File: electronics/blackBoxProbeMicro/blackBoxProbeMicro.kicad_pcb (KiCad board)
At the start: 4 copper layers, 29 x 29 mm, 60 parts, among them J1 USB-C, J2 JTAG_2X05, J3 JTAG_2X05, J4 DevBoardUartOutput, Q1 Q_NMOS_DUAL, Q2 Q_PMOS_DUAL, U1 MCP1702-MB, U2 USBLC6-2, U3 STM32F103CBT, Y1 8MHz

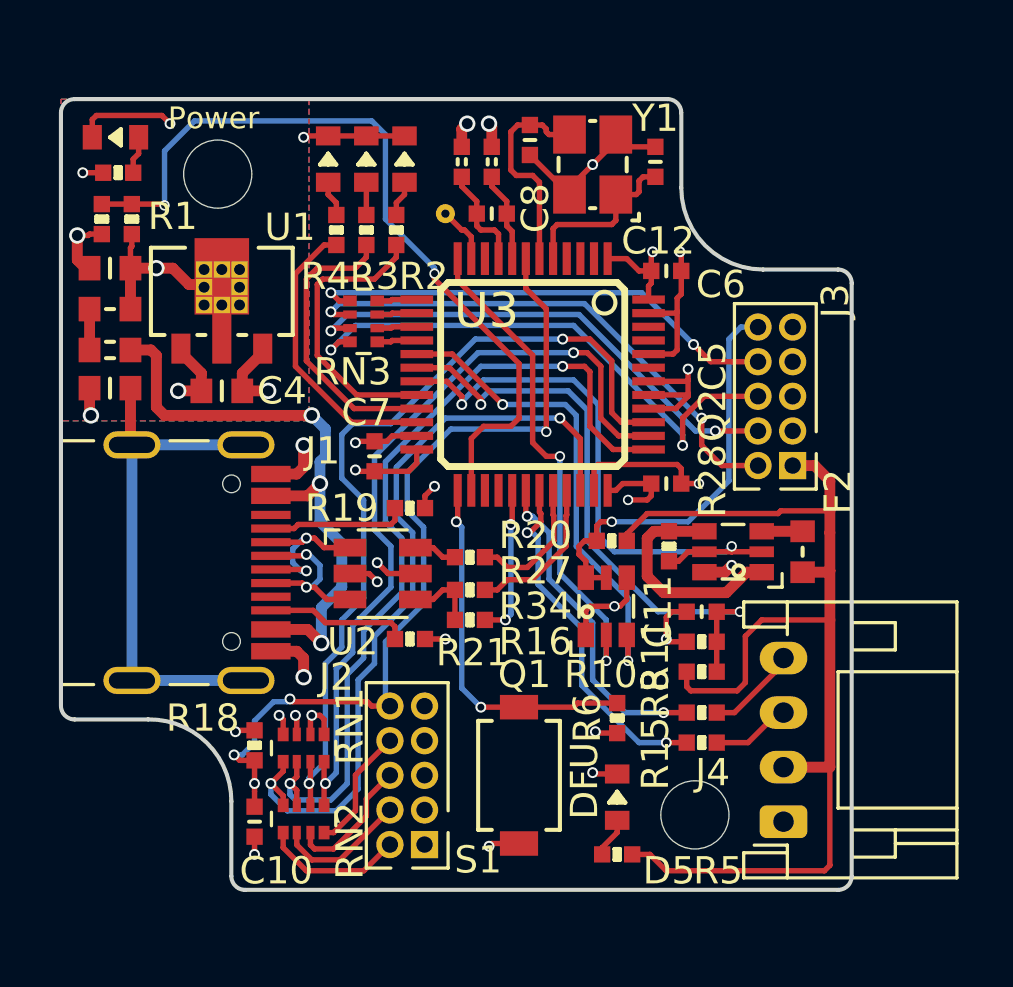
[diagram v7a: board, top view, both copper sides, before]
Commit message: further silk and routing optimizations
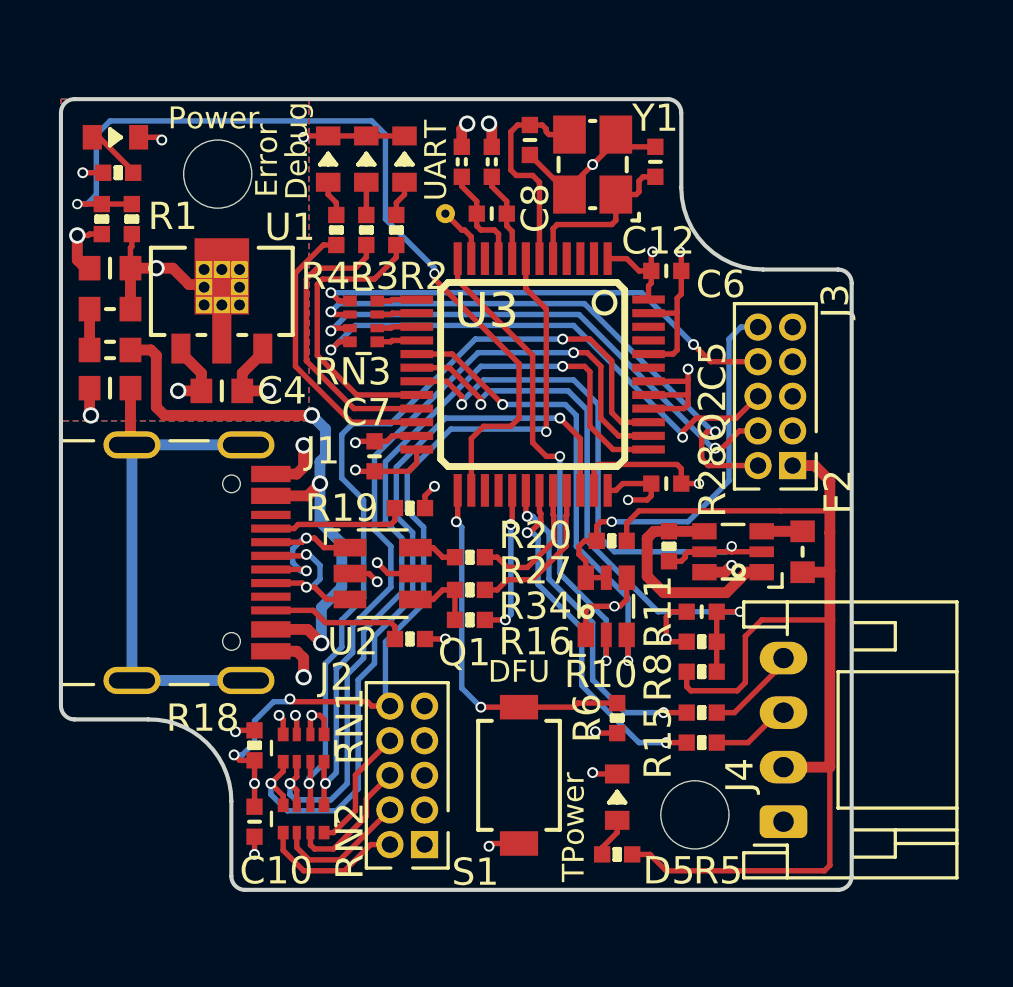
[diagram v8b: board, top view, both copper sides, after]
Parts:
- turned D1 to 180 degrees
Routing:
- net /USB_V: track 29.5 -> 32.4 mm
- net /VSS: track 50.7 -> 47.9 mm
- net /PROBE_E_TDO: track 20.3 -> 19.4 mm
- net /PROBE_E_TMS: track 19.6 -> 20.5 mm
- net Net-(D1-Pad2): track 1.38 -> 2.07 mm
- net /PROBE_E_TCK: track 18.4 -> 18.9 mm
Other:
- board text added: "Debug"
- board text added: "Error"
- board text added: "TPower"
- board text added: "UART"
